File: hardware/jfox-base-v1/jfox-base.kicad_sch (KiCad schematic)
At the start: 0 parts

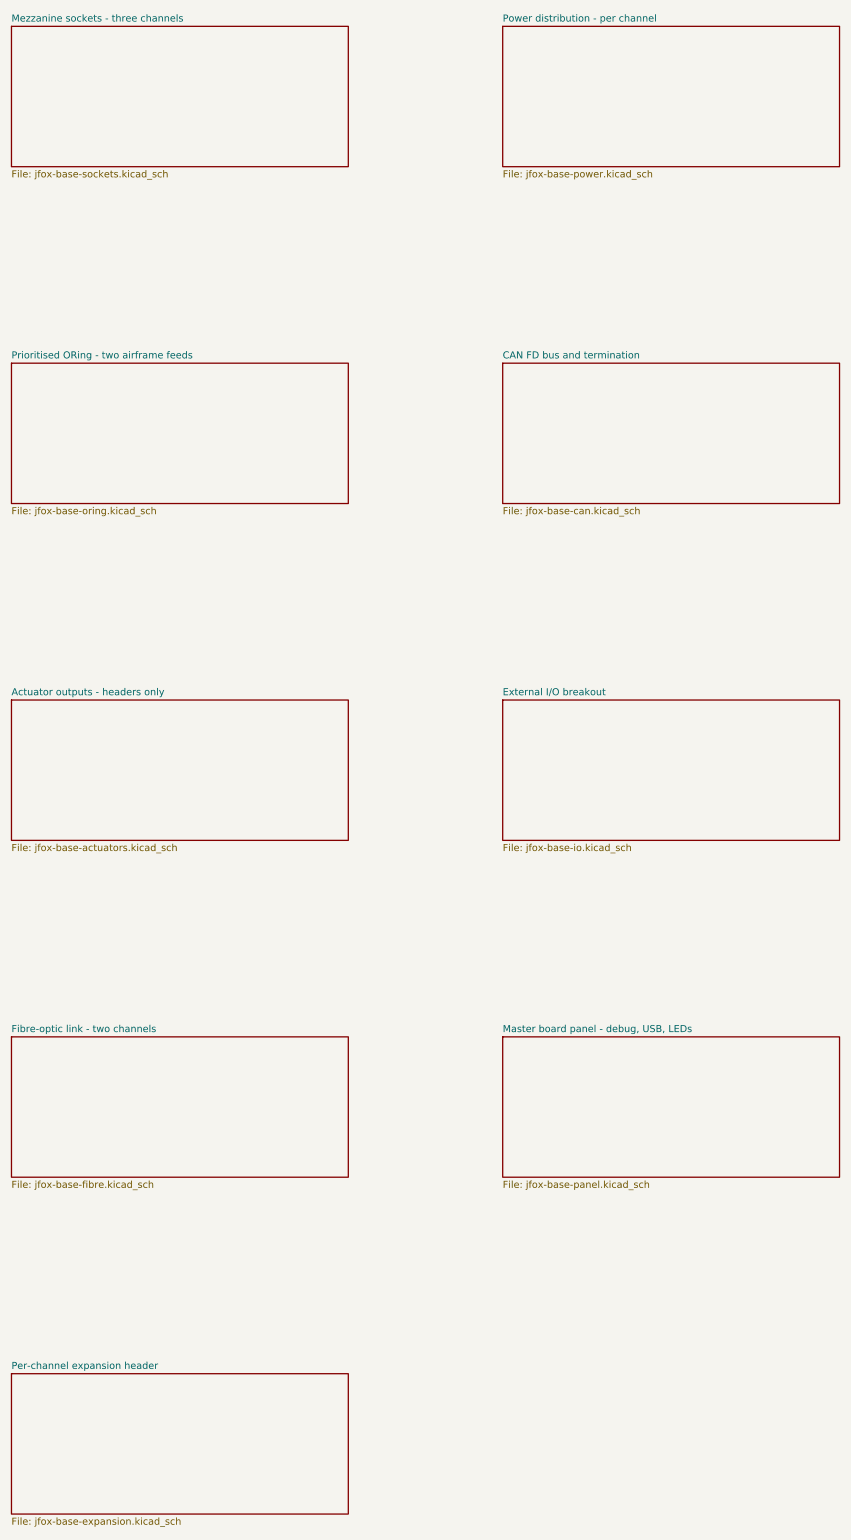
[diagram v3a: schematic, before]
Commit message: DO-160G protection stage, and a check that recognises parts not labels
Series inductance and an SMCJ clamp on each airframe feed, bulk on the ORed
rail, soft-start per slot. Order is deliberate - L, clamp, ORing, bulk - as
a TVS with nothing ahead of it absorbs the whole injected transient itself,
which is how a correctly chosen part still fails.

ASSUMED: section 22 pin injection LEVEL 3. It was not specified, so it is
recorded in the sheet note and in VOLTAGE_ANALYSIS.md rather than left
implicit. Level 4 or 5 need larger parts than these.

SECTION 16 POWER INTERRUPT IS NOT MET, and the arithmetic is why. Three
cards at 1.2 A riding 5.16 V down to 4.50 V need 1.8 mF for 1 ms and 364 mF
for 200 ms. 364 mF at 5 V is a supercapacitor bank. C60 is sized for the
feed-to-feed switchover the ORing stage itself creates, about 1 ms, and the
interrupt is declared not met. Meeting it means holding up at a higher
voltage ahead of the ORing or requiring the airframe to provide it - both
decisions above this board. Sizing for the case you can meet and letting the
requirement imply the other is how this goes wrong quietly.

D50/D51 retained. With the LTC4417's back-to-back pairs they are redundant
for SELECTION and cost ~0.4 V, but the pass FETs only block reverse current
in the orientation the controller drives them, and a feed connected
backwards is exactly the case where the controller has no say.

The check that verifies all this had the flaw this session keeps producing.
It tested `r.startswith("D")` - a reference designator prefix - so a board
whose clamps had been replaced by 0R resistors passed, because D60 was still
called D60. A refdes is a label someone chose; the value is what gets
fitted. It now matches against known clamp families and inductance forms,
and the negative test fails on the right line.

The inductance matcher was wrong too on first attempt: it required a
trailing H, and inductance is written 10u on a BOM, not 10uH. It rejected
every real value and repo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
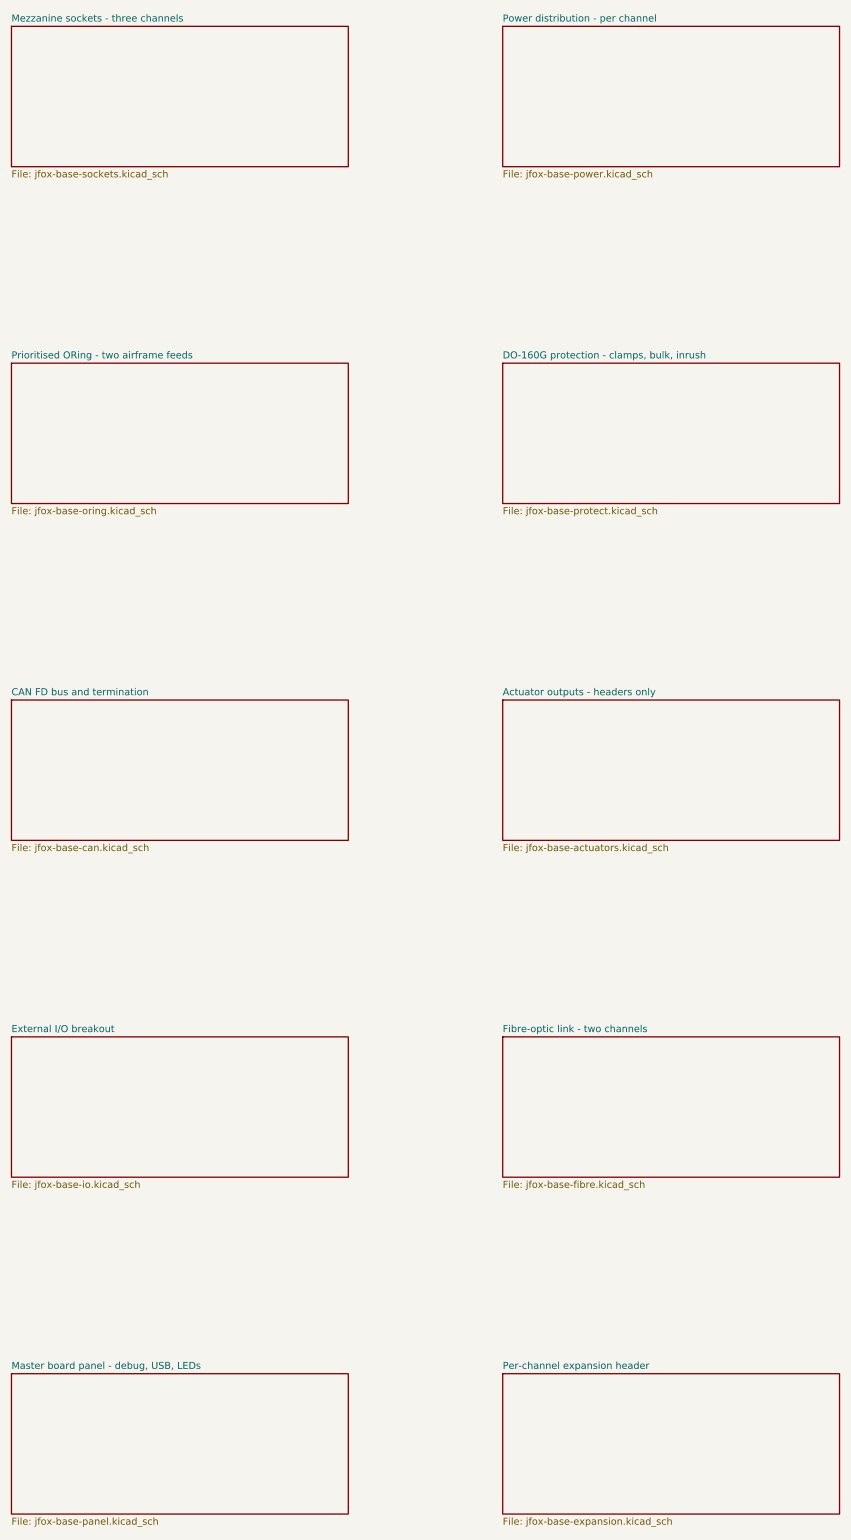
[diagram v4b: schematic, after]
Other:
- added sheet DO-160G protection - clamps, bulk, inrush (jfox-base-protect.kicad_sch)
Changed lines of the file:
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@@
 		(instances
 			(project "jfox-base"
-				(path "/ad7e3dd9-f5c3-4a31-b83a-a44a809bac12"
+				(path "/4e8351d0-910d-4549-86a1-59a591717b0d"
 					(page "2")
 				)
@@
 		(instances
 			(project "jfox-base"
-				(path "/ad7e3dd9-f5c3-4a31-b83a-a44a809bac12"
+				(path "/4e8351d0-910d-4549-86a1-59a591717b0d"
 					(page "3")
 				)
@@
 		(instances
 			(project "jfox-base"
-				(path "/ad7e3dd9-f5c3-4a31-b83a-a44a809bac12"
+				(path "/4e8351d0-910d-4549-86a1-59a591717b0d"
 					(page "4")
 				)
@@
 		(stroke (width 0.1524)(type solid))
 		(fill (color 0 0 0 0.0000))
+		(property "Sheetname" "DO-160G protection - clamps, bulk, inrush"
+			(at 114.30000000000001 100.89 0)
+			(effects (font (size 1.27 1.27))(justify left bottom))
+		)
+		(property "Sheetfile" "jfox-base-protect.kicad_sch"
+			(at 114.30000000000001 127.6 0)
+			(effects (font (size 1.27 1.27))(justify left top))
+		)
+		(instances
+			(project "jfox-base"
+				(path "/4e8351d0-910d-4549-86a1-59a591717b0d"
+					(page "5")
+				)
+			)
+		)
+	)
+	(sheet
+		(at 25.4 162.56)
+		(size 60.96 25.4)
+		(fields_autoplaced yes)
+		(stroke (width 0.1524)(type solid))
+		(fill (color 0 0 0 0.0000))
 		(property "Sheetname" "CAN FD bus and termination"
-			(at 114.30000000000001 100.89 0)
+			(at 25.4 161.85 0)
 			(effects (font (size 1.27 1.27))(justify left bottom))
 		)
 		(property "Sheetfile" "jfox-base-can.kicad_sch"
-			(at 114.30000000000001 127.6 0)
-			(effects (font (size 1.27 1.27))(justify left top))
-		)
-		(instances
-			(project "jfox-base"
-				(path "/ad7e3dd9-f5c3-4a31-b83a-a44a809bac12"
-					(page "5")
-				)
-			)
-		)
-	)
-	(sheet
-		(at 25.4 162.56)
+			(at 25.4 188.56 0)
+			(effects (font (size 1.27 1.27))(justify left top))
+		)
+		(instances
+			(project "jfox-base"
+				(path "/4e8351d0-910d-4549-86a1-59a591717b0d"
+					(page "6")
+				)
+			)
+		)
+	)
+	(sheet
+		(at 114.30000000000001 162.56)
 		(size 60.96 25.4)
 		(fields_autoplaced yes)
@@
 		(fill (color 0 0 0 0.0000))
 		(property "Sheetname" "Actuator outputs - headers only"
-			(at 25.4 161.85 0)
+			(at 114.30000000000001 161.85 0)
 			(effects (font (size 1.27 1.27))(justify left bottom))
 		)
 		(property "Sheetfile" "jfox-base-actuators.kicad_sch"
-			(at 25.4 188.56 0)
-			(effects (font (size 1.27 1.27))(justify left top))
-		)
-		(instances
-			(project "jfox-base"
-				(path "/ad7e3dd9-f5c3-4a31-b83a-a44a809bac12"
-					(page "6")
-				)
-			)
-		)
-	)
-	(sheet
-		(at 114.30000000000001 162.56)
+			(at 114.30000000000001 188.56 0)
+			(effects (font (size 1.27 1.27))(justify left top))
+		)
+		(instances
+			(project "jfox-base"
+				(path "/4e8351d0-910d-4549-86a1-59a591717b0d"
+					(page "7")
+				)
+			)
+		)
+	)
+	(sheet
+		(at 25.4 223.51999999999998)
 		(size 60.96 25.4)
 		(fields_autoplaced yes)
@@
 		(fill (color 0 0 0 0.0000))
 		(property "Sheetname" "External I/O breakout"
-			(at 114.30000000000001 161.85 0)
+			(at 25.4 222.81 0)
 			(effects (font (size 1.27 1.27))(justify left bottom))
 		)
 		(property "Sheetfile" "jfox-base-io.kicad_sch"
-			(at 114.30000000000001 188.56 0)
-			(effects (font (size 1.27 1.27))(justify left top))
-		)
-		(instances
-			(project "jfox-base"
-				(path "/ad7e3dd9-f5c3-4a31-b83a-a44a809bac12"
-					(page "7")
-				)
-			)
-		)
-	)
-	(sheet
-		(at 25.4 223.51999999999998)
+			(at 25.4 249.52 0)
+			(effects (font (size 1.27 1.27))(justify left top))
+		)
+		(instances
+			(project "jfox-base"
+				(path "/4e8351d0-910d-4549-86a1-59a591717b0d"
+					(page "8")
+				)
+			)
+		)
+	)
+	(sheet
+		(at 114.30000000000001 223.51999999999998)
 		(size 60.96 25.4)
 		(fields_autoplaced yes)
@@
 		(fill (color 0 0 0 0.0000))
 		(property "Sheetname" "Fibre-optic link - two channels"
-			(at 25.4 222.81 0)
+			(at 114.30000000000001 222.81 0)
 			(effects (font (size 1.27 1.27))(justify left bottom))
 		)
 		(property "Sheetfile" "jfox-base-fibre.kicad_sch"
-			(at 25.4 249.52 0)
-			(effects (font (size 1.27 1.27))(justify left top))
-		)
-		(instances
-			(project "jfox-base"
-				(path "/ad7e3dd9-f5c3-4a31-b83a-a44a809bac12"
-					(page "8")
-				)
-			)
-		)
-	)
-	(sheet
-		(at 114.30000000000001 223.51999999999998)
+			(at 114.30000000000001 249.52 0)
+			(effects (font (size 1.27 1.27))(justify left top))
+		)
+		(instances
+			(project "jfox-base"
+				(path "/4e8351d0-910d-4549-86a1-59a591717b0d"
+					(page "9")
+				)
+			)
+		)
+	)
+	(sheet
+		(at 25.4 284.48)
 		(size 60.96 25.4)
 		(fields_autoplaced yes)
@@
 		(fill (color 0 0 0 0.0000))
 		(property "Sheetname" "Master board panel - debug, USB, LEDs"
-			(at 114.30000000000001 222.81 0)
+			(at 25.4 283.77 0)
 			(effects (font (size 1.27 1.27))(justify left bottom))
 		)
 		(property "Sheetfile" "jfox-base-panel.kicad_sch"
-			(at 114.30000000000001 249.52 0)
-			(effects (font (size 1.27 1.27))(justify left top))
-		)
-		(instances
-			(project "jfox-base"
-				(path "/ad7e3dd9-f5c3-4a31-b83a-a44a809bac12"
-					(page "9")
-				)
-			)
-		)
-	)
-	(sheet
-		(at 25.4 284.48)
+			(at 25.4 310.48 0)
+			(effects (font (size 1.27 1.27))(justify left top))
+		)
+		(instances
+			(project "jfox-base"
+				(path "/4e8351d0-910d-4549-86a1-59a591717b0d"
+					(page "10")
+				)
+			)
+		)
+	)
+	(sheet
+		(at 114.30000000000001 284.48)
 		(size 60.96 25.4)
 		(fields_autoplaced yes)
@@
 		(fill (color 0 0 0 0.0000))
 		(property "Sheetname" "Per-channel expansion header"
-			(at 25.4 283.77 0)
+			(at 114.30000000000001 283.77 0)
 			(effects (font (size 1.27 1.27))(justify left bottom))
 		)
 		(property "Sheetfile" "jfox-base-expansion.kicad_sch"
-			(at 25.4 310.48 0)
-			(effects (font (size 1.27 1.27))(justify left top))
-		)
-		(instances
-			(project "jfox-base"
-				(path "/ad7e3dd9-f5c3-4a31-b83a-a44a809bac12"
-					(page "10")
-				)
-			)
+			(at 114.30000000000001 310.48 0)
+			(effects (font (size 1.27 1.27))(justify left top))
+		)
+		(instances
+			(project "jfox-base"
+				(path "/4e8351d0-910d-4549-86a1-59a591717b0d"
+					(page "11")
+				)
+			)
